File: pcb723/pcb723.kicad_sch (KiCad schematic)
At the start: 59 parts, among them J1 Conn_01x02_Pin, J2 Conn_01x02_Pin, J3 Conn_02x07_Odd_Even, J4 Conn_02x04_Odd_Even, J5 USB_C_Receptacle_USB2.0_16P, J6 Conn_02x13_Odd_Even, J7 Conn_02x14_Odd_Even, SW1 SW_Push, U1 STM32H723ZGT6, U2 AMS1117-3.3, Y1 8MHz 20pF

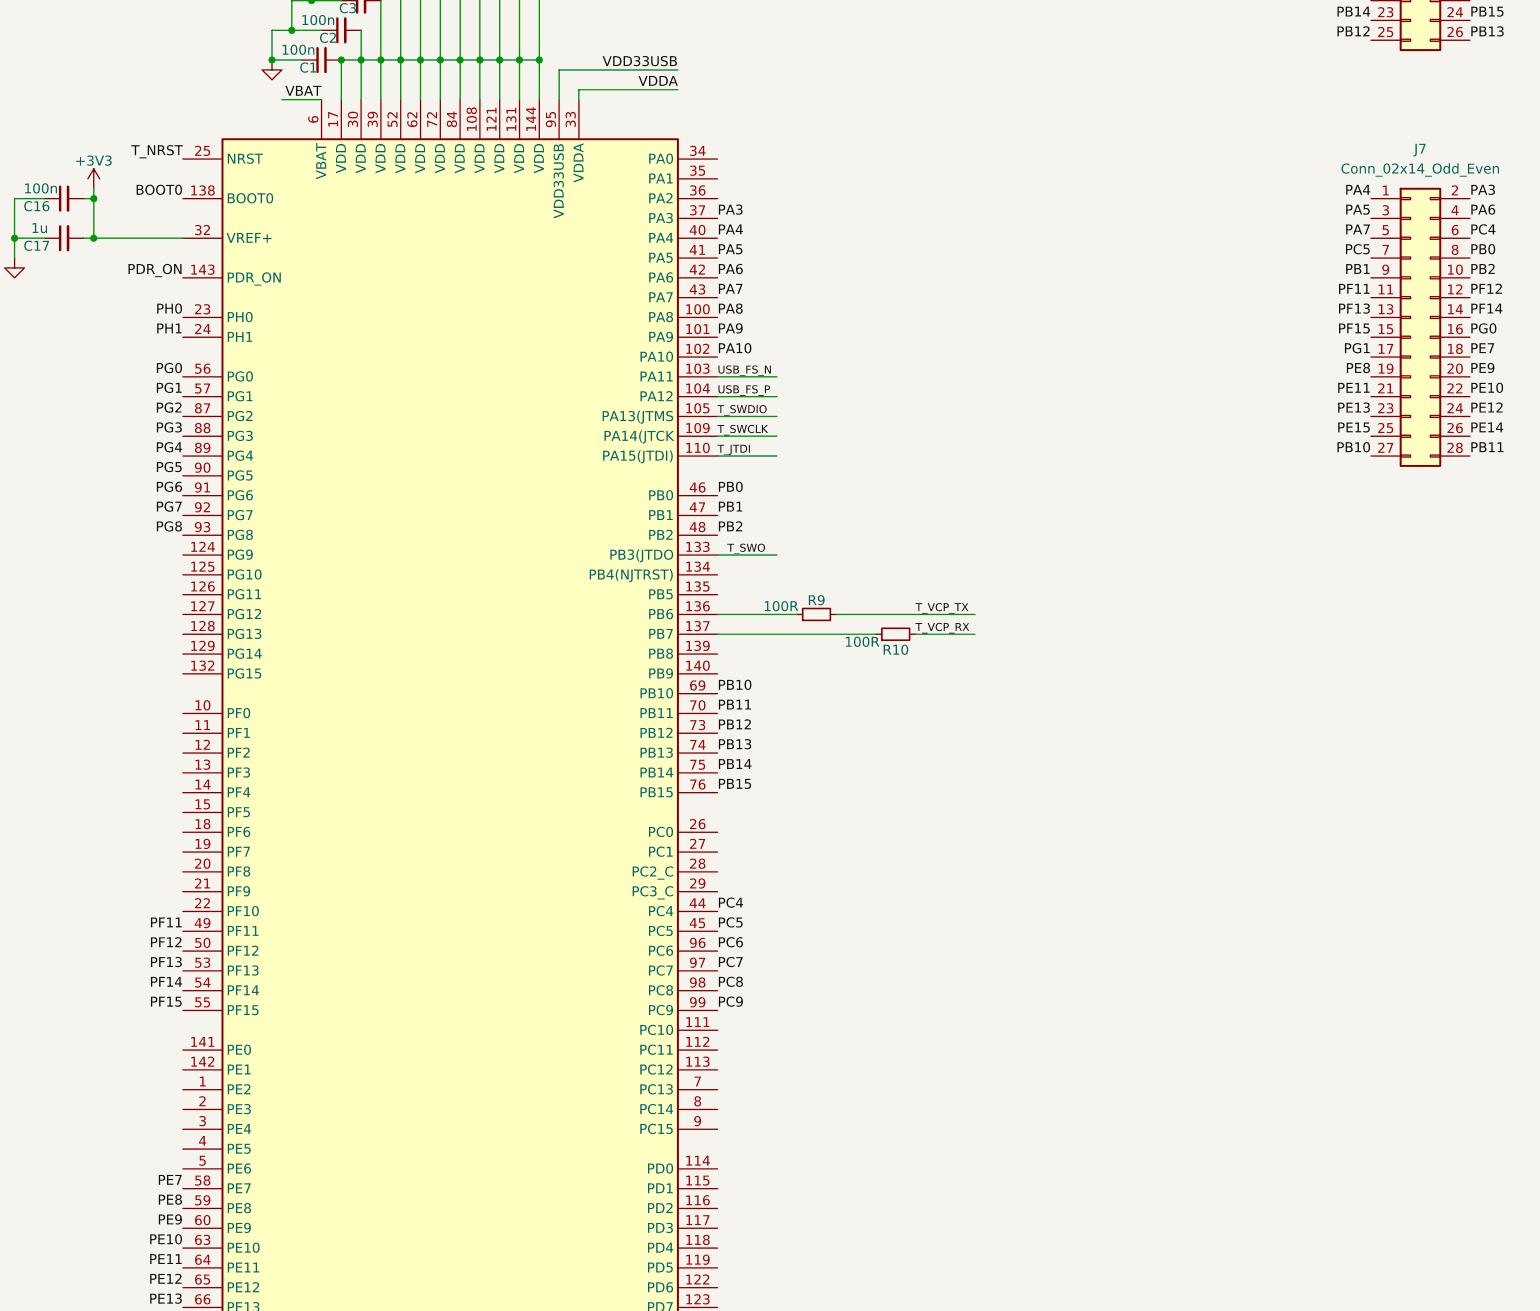
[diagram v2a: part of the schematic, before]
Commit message: Add left breakout connector
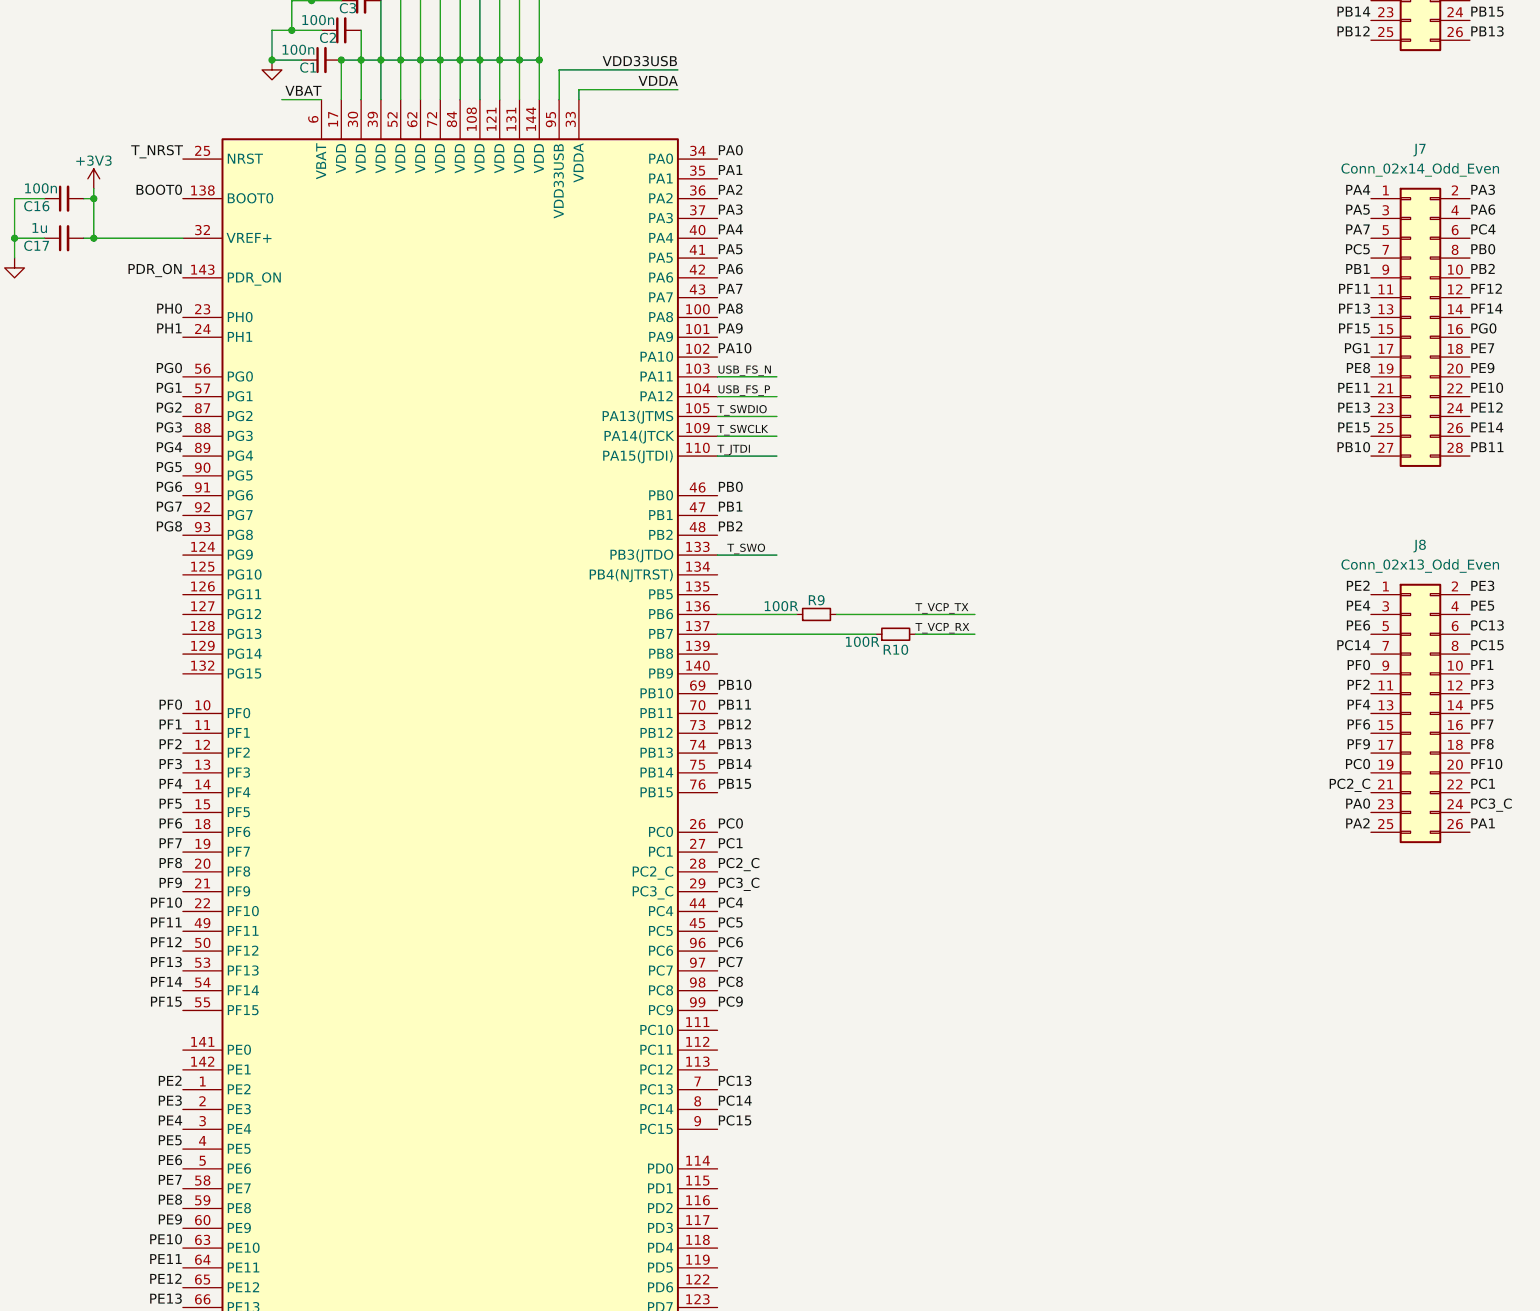
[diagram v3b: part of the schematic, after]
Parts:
- added J8: Conn_02x13_Odd_Even, Connector_PinSocket_2.54mm:PinSocket_2x13_P2.54mm_Vertical, symbol Connector_Generic:Conn_02x13_Odd_Even
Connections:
- net PE2: now reaches U1.1 (PE2)
- net PE2: now also J8.1 (Pin_1)
- net PF0: now reaches U1.10 (PF0)
- net PF0: now also J8.9 (Pin_9)
- net PF1: now reaches U1.11 (PF1)
- net PF1: now also J8.10 (Pin_10)
- net PF2: now reaches U1.12 (PF2)
- net PF2: now also J8.11 (Pin_11)
- net PF3: now reaches U1.13 (PF3)
- net PF3: now also J8.12 (Pin_12)
- net PF4: now reaches U1.14 (PF4)
- net PF4: now also J8.13 (Pin_13)
- net PF5: now reaches U1.15 (PF5)
- net PF5: now also J8.14 (Pin_14)
- net PF6: now reaches U1.18 (PF6)
- net PF6: now also J8.15 (Pin_15)
- net PF7: now reaches U1.19 (PF7)
- net PF7: now also J8.16 (Pin_16)
- net PE3: now reaches U1.2 (PE3)
- net PE3: now also J8.2 (Pin_2)
- net PF8: now reaches U1.20 (PF8)
- net PF8: now also J8.18 (Pin_18)
- net PF9: now reaches U1.21 (PF9)
- net PF9: now also J8.17 (Pin_17)
- net PF10: now reaches U1.22 (PF10)
- net PF10: now also J8.20 (Pin_20)
- net PC0: now reaches U1.26 (PC0)
- net PC0: now also J8.19 (Pin_19)
- net PC1: now reaches U1.27 (PC1)
- net PC1: now also J8.22 (Pin_22)
- net PC2_C: now reaches U1.28 (PC2_C)
- net PC2_C: now also J8.21 (Pin_21)
- net PC3_C: now reaches U1.29 (PC3_C)
- net PC3_C: now also J8.24 (Pin_24)
- net PE4: now reaches U1.3 (PE4)
- net PE4: now also J8.3 (Pin_3)
- net PA0: now reaches U1.34 (PA0)
- net PA0: now also J8.23 (Pin_23)
- net PA1: now reaches U1.35 (PA1)
- net PA1: now also J8.26 (Pin_26)
- net PA2: now reaches U1.36 (PA2)
- net PA2: now also J8.25 (Pin_25)
- net PE5: now reaches U1.4 (PE5)
- net PE5: now also J8.4 (Pin_4)
- net PE6: now reaches U1.5 (PE6)
- net PE6: now also J8.5 (Pin_5)
- net PC13: now reaches U1.7 (PC13)
- net PC13: now also J8.6 (Pin_6)
- net PC14: now reaches U1.8 (PC14)
- net PC14: now also J8.7 (Pin_7)
- net PC15: now reaches U1.9 (PC15)
- net PC15: now also J8.8 (Pin_8)

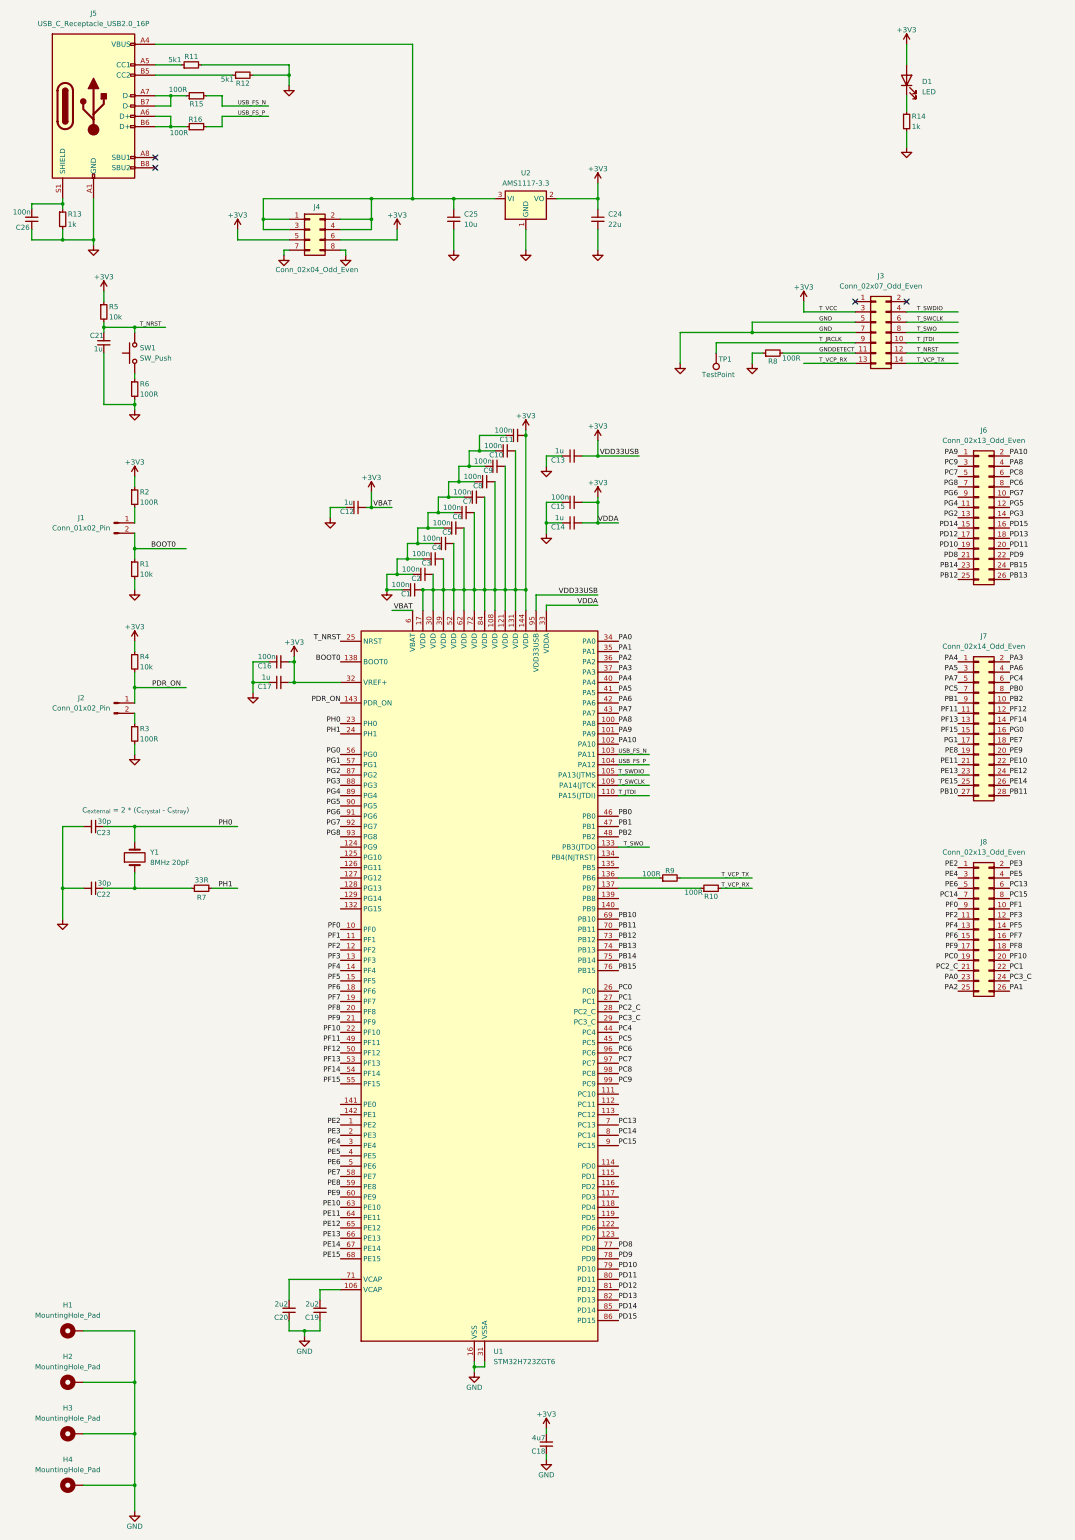
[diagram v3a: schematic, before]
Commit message: Add 24 pin socket
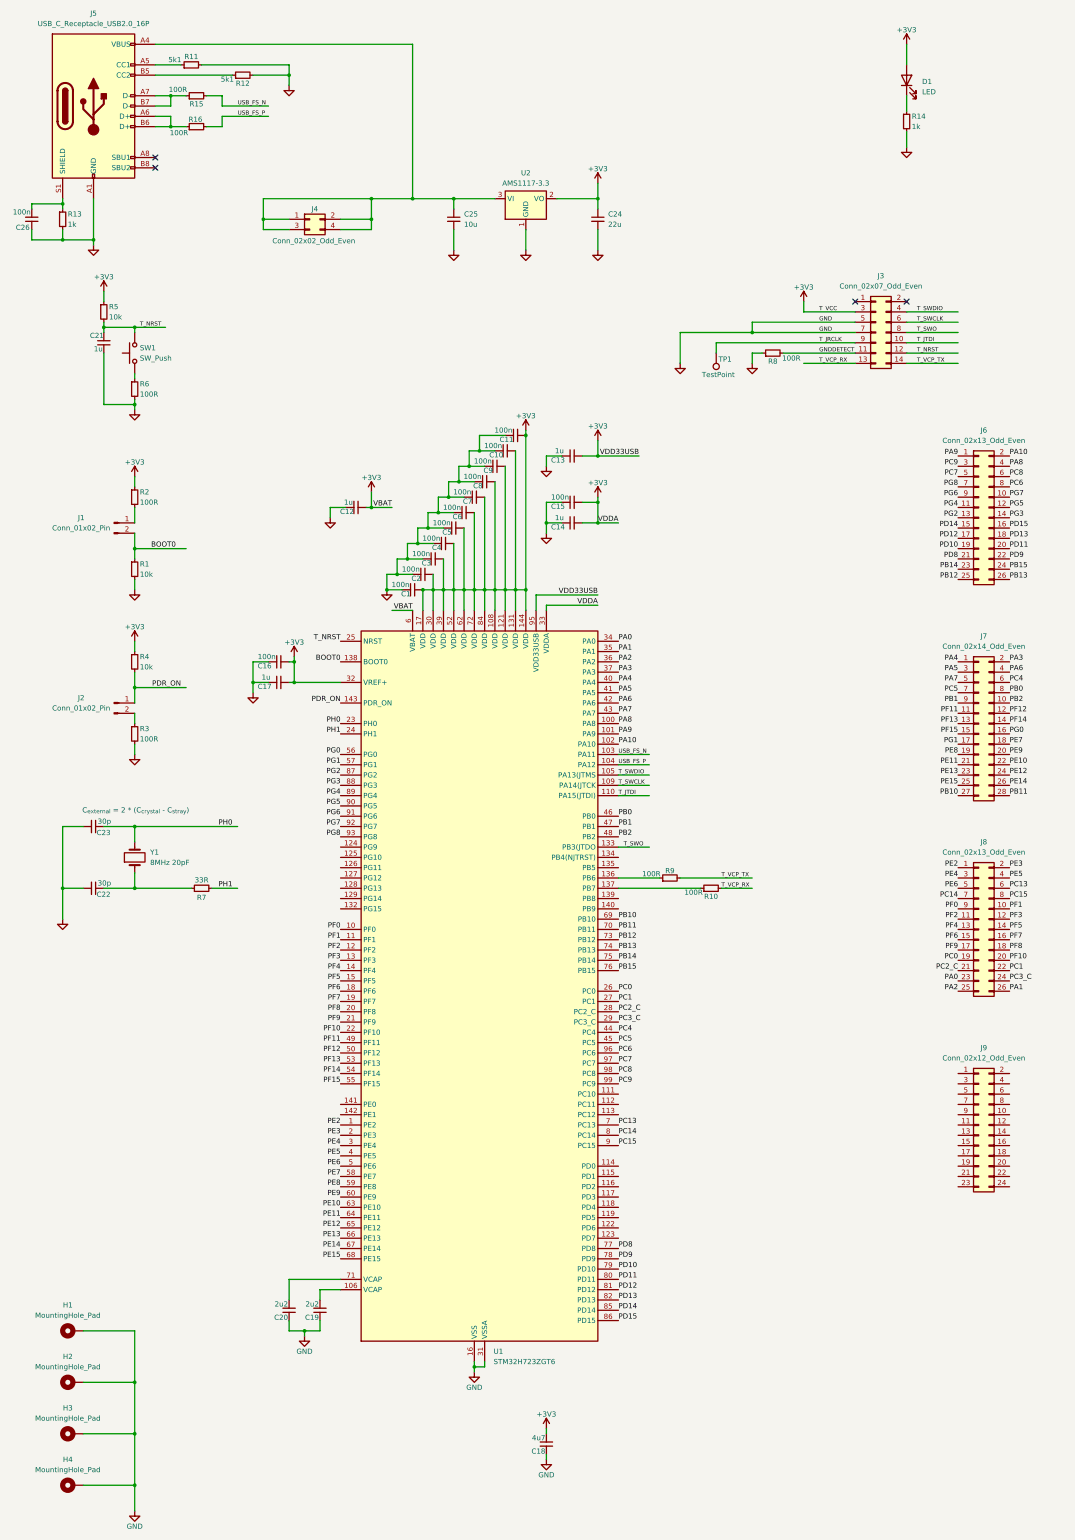
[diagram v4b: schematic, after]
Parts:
- removed J4: Conn_02x04_Odd_Even, Connector_PinSocket_2.54mm:PinSocket_2x04_P2.54mm_Vertical, symbol Connector_Generic:Conn_02x04_Odd_Even
- added J4: Conn_02x02_Odd_Even, Connector_PinSocket_2.54mm:PinSocket_2x02_P2.54mm_Vertical, symbol Connector_Generic:Conn_02x02_Odd_Even
- added J9: Conn_02x12_Odd_Even, Connector_PinSocket_2.54mm:PinSocket_2x12_P2.54mm_Vertical, symbol Connector_Generic:Conn_02x12_Odd_Even
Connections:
- net at C25.1, J5.A4 (VBUS), J5.A9 (VBUS)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: now also J4.1 (Pin_1), J4.2 (Pin_2), J4.3 (Pin_3), J4.4 (Pin_4)
